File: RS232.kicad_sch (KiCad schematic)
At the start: 12 parts, among them Q5 BSS84, Q6 BSS84, U9 MAX3227

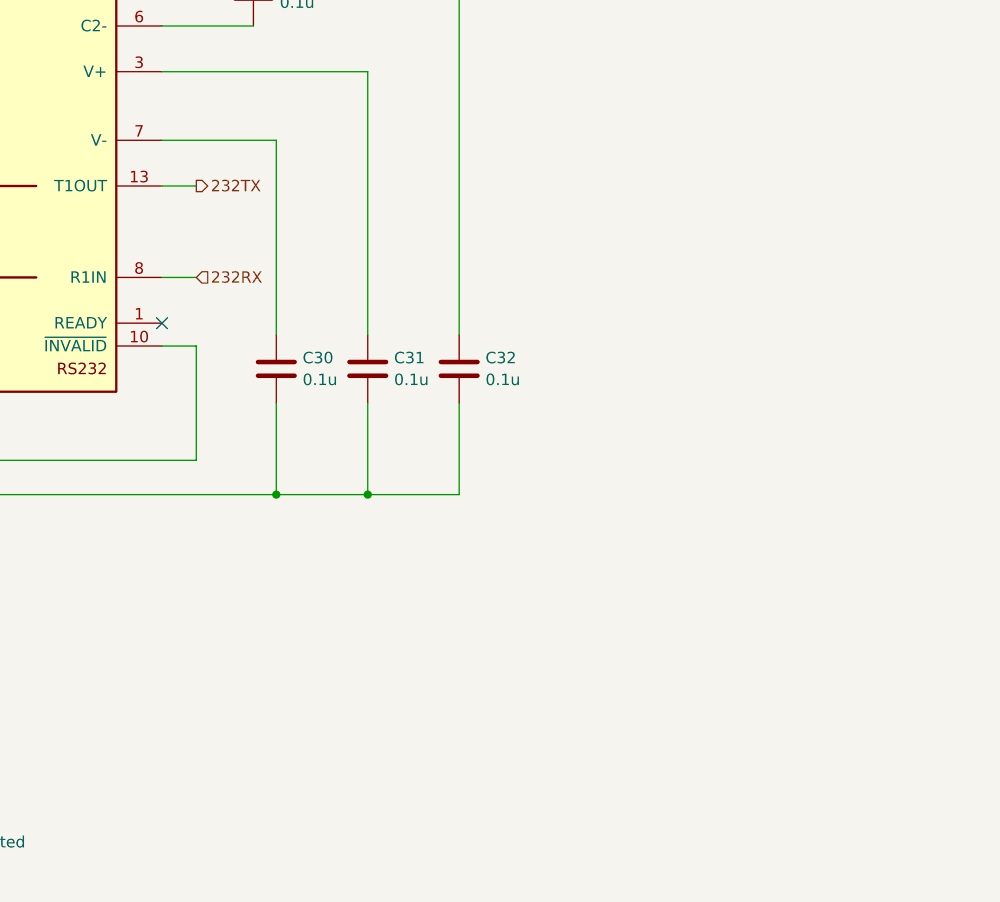
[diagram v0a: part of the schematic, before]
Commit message: added 4 inputs and 2 pwm outputs, completed routing
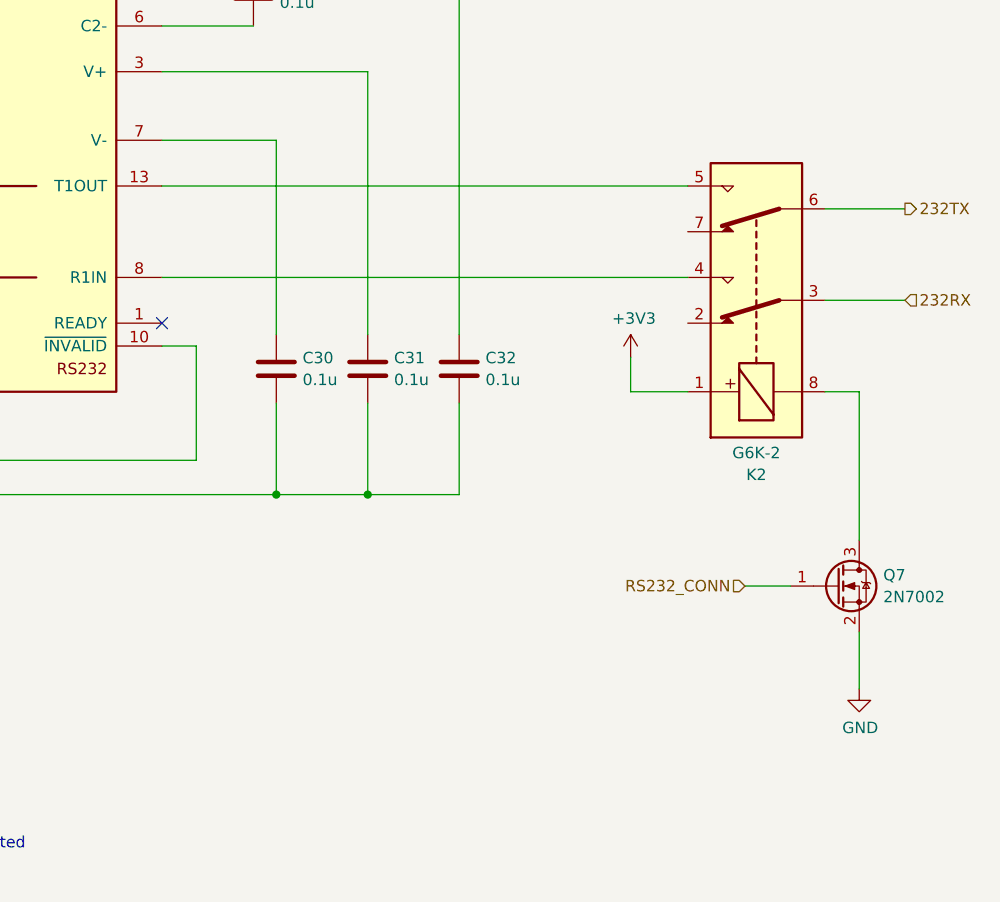
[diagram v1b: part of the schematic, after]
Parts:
- added K2: G6K-2, Relay_SMD:Relay_DPDT_Omron_G6K-2F, symbol Relay:G6K-2
- added Q7: 2N7002, Package_TO_SOT_SMD:SOT-23, symbol Transistor_FET:2N7002
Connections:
- net +3V3: now also K2.1
- net 232RX: now also K2.3; no longer U9.8 (R1IN)
- net 232TX: now also K2.6; no longer U9.13 (T1OUT)
- net GND: now also Q7.2 (S)
- new net: K2.5, U9.13 (T1OUT)
- new net: K2.4, U9.8 (R1IN)
- new net: K2.8, Q7.3 (D)
- new net RS232_CONN: Q7.1 (G)

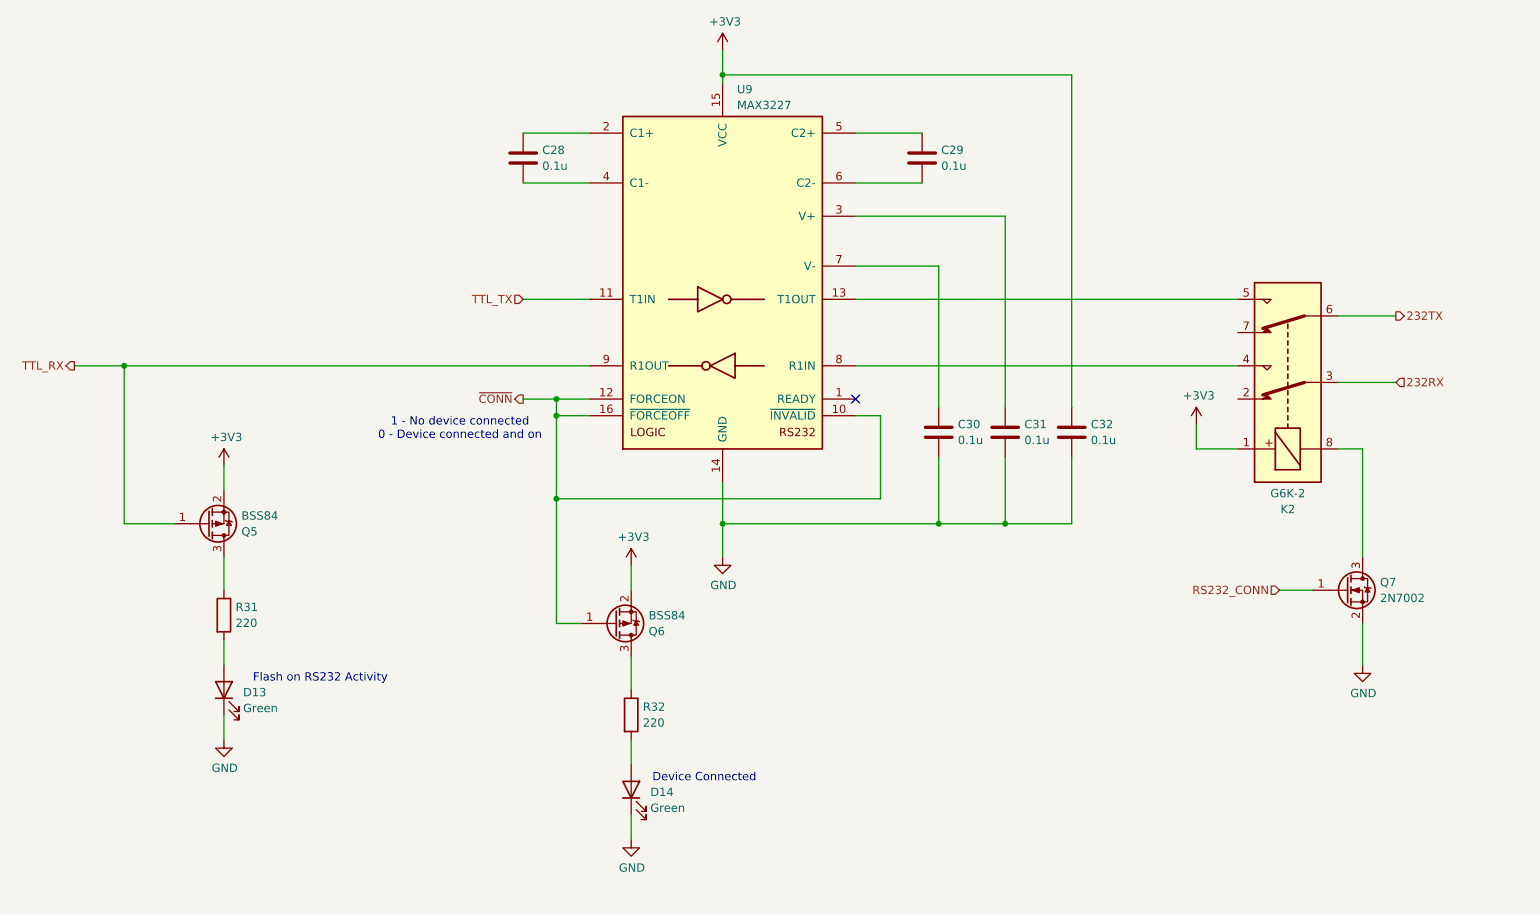
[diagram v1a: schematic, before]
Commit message: revised schematic after initial layout  - all connectors are vertical  - increased current handling of outputs  - replaced mechanical relay with ssr  - jumper to disable gps antenna power
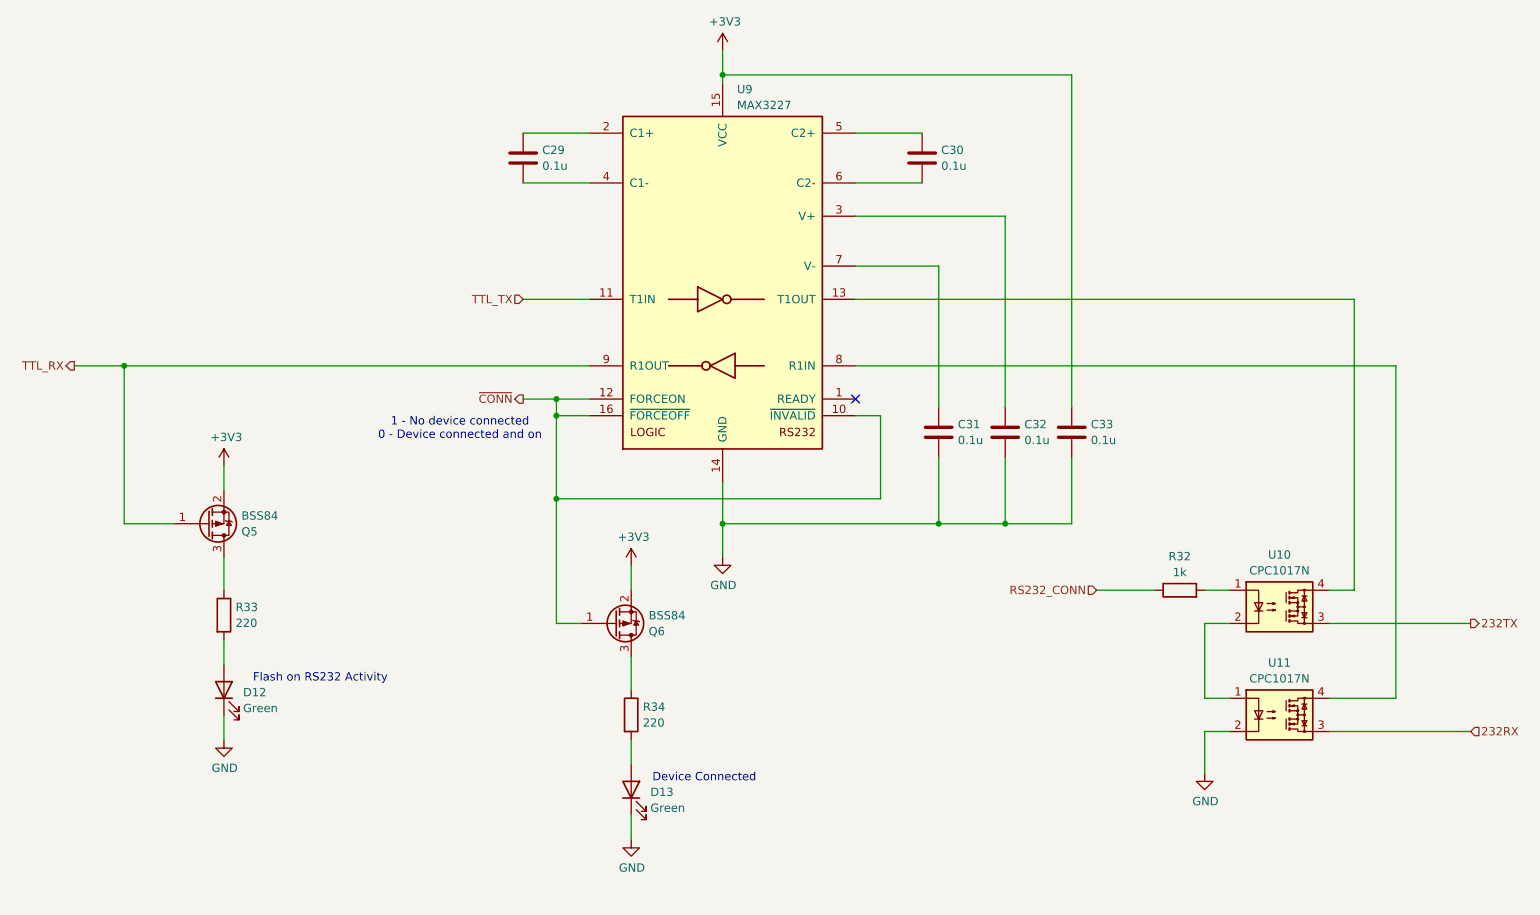
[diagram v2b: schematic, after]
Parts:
- removed K2: G6K-2, Relay_SMD:Relay_DPDT_Omron_G6K-2F, symbol Relay:G6K-2
- removed Q7: 2N7002, Package_TO_SOT_SMD:SOT-23, symbol Transistor_FET:2N7002
- added R32: 1k, Resistor_SMD:R_0603_1608Metric, symbol Device:R
- added U10, U11: CPC1017N, Package_SO:SOP-4_3.8x4.1mm_P2.54mm, symbol Relay_SolidState:CPC1017N
- C29: renamed from C28; footprint Capacitor_SMD:C_0603_1608Metric_Pad1.08x0.95mm_HandSolder -> Capacitor_SMD:C_0603_1608Metric
- C30: renamed from C29; footprint Capacitor_SMD:C_0603_1608Metric_Pad1.08x0.95mm_HandSolder -> Capacitor_SMD:C_0603_1608Metric
- C31: renamed from C30; footprint Capacitor_SMD:C_0603_1608Metric_Pad1.08x0.95mm_HandSolder -> Capacitor_SMD:C_0603_1608Metric
- C32: renamed from C31; footprint Capacitor_SMD:C_0603_1608Metric_Pad1.08x0.95mm_HandSolder -> Capacitor_SMD:C_0603_1608Metric
- C33: renamed from C32; footprint Capacitor_SMD:C_0603_1608Metric_Pad1.08x0.95mm_HandSolder -> Capacitor_SMD:C_0603_1608Metric
- D12: renamed from D13; footprint LED_SMD:LED_0603_1608Metric_Pad1.05x0.95mm_HandSolder -> LED_SMD:LED_0603_1608Metric
- D13: renamed from D14; footprint LED_SMD:LED_0603_1608Metric_Pad1.05x0.95mm_HandSolder -> LED_SMD:LED_0603_1608Metric
- R33: renamed from R31; footprint Resistor_SMD:R_0603_1608Metric_Pad0.98x0.95mm_HandSolder -> Resistor_SMD:R_0603_1608Metric
- R34: renamed from R32; footprint Resistor_SMD:R_0603_1608Metric_Pad0.98x0.95mm_HandSolder -> Resistor_SMD:R_0603_1608Metric
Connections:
- net 232RX: now also U11.3
- net 232TX: now also U10.3
- net GND: now also U11.2
- net RS232_CONN: now also R32.1
- net at U9.13 (T1OUT): now also U10.4
- net at U9.8 (R1IN): now also U11.4
- new net: R32.2, U10.1
- new net: U10.2, U11.1

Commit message: second pass at layout complete
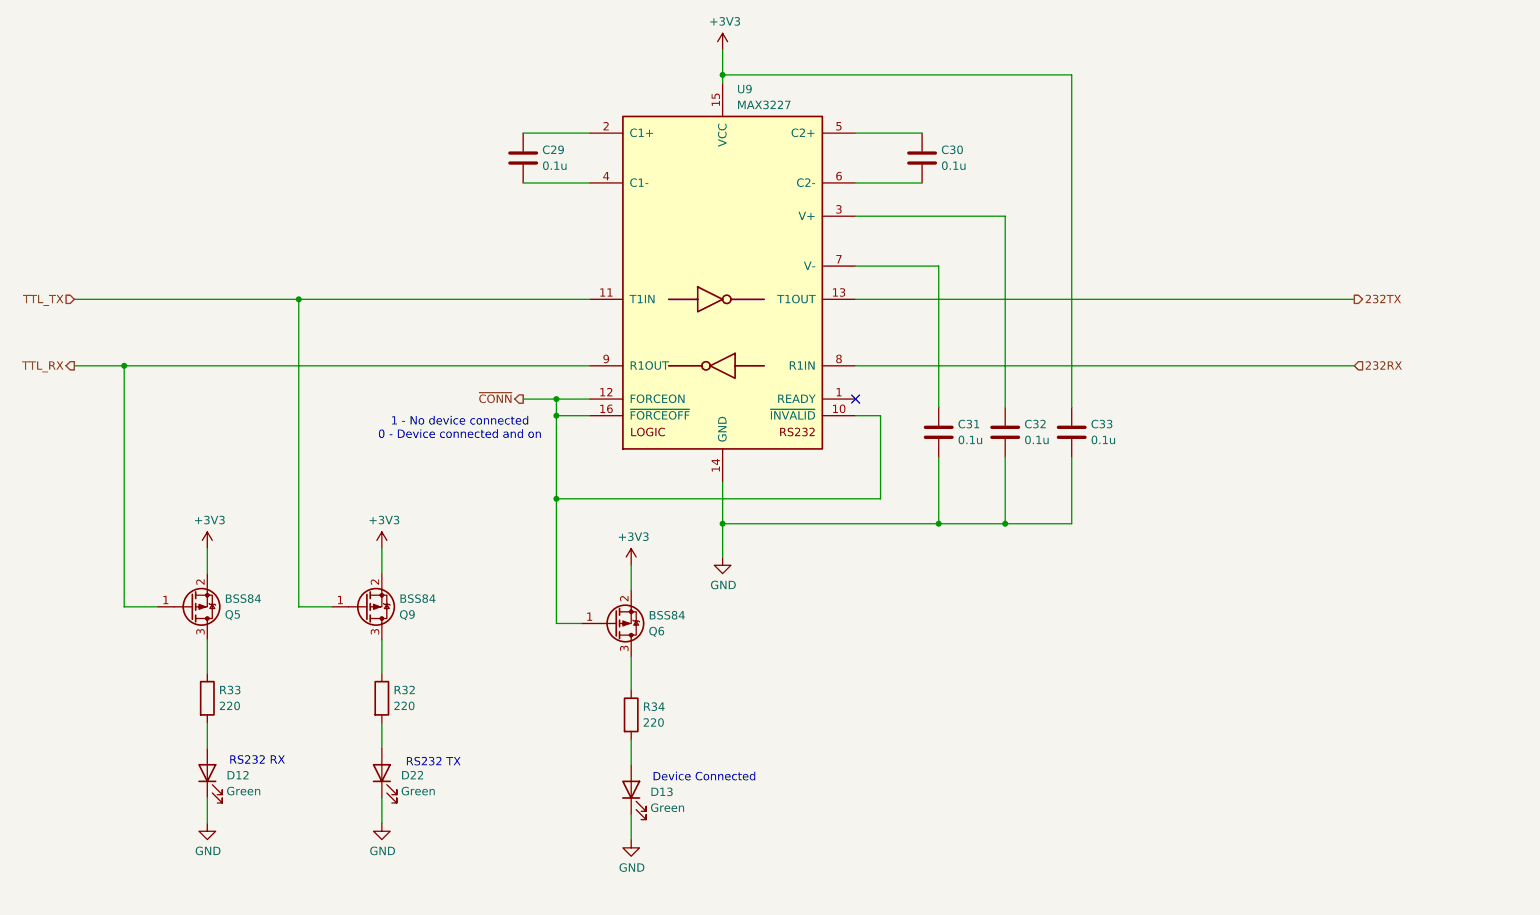
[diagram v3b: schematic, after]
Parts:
- removed U10, U11: CPC1017N, Package_SO:SOP-4_3.8x4.1mm_P2.54mm, symbol Relay_SolidState:CPC1017N
- added D22: Green, LED_SMD:LED_0603_1608Metric, symbol Device:LED
- added Q9: BSS84, Package_TO_SOT_SMD:SOT-23, symbol Transistor_FET:BSS84
- R32: value 1k -> 220
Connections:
- net +3V3: now also Q9.2 (S)
- net 232RX: now also U9.8 (R1IN)
- net 232TX: now also U9.13 (T1OUT)
- net GND: now also D22.1 (K)
- net TTL_TX: now also Q9.1 (G)
- net at R32.2: now also D22.2 (A)
- net RS232_CONN: no longer names the net of R32.1
- net RS232_CONN: now also Q9.3 (D)
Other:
- note added: "RS232 RX"
- note added: "RS232 TX"
- note removed: "Flash on RS232 Activity"
- moved on the sheet: D12, Q5, R33

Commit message: add a version, add uart test pads to gps, sent for manufacturing
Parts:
- Q5, Q6, Q9: Mfg Part Number BSS84 -> 2N7002
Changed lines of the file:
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@@
 			)
 		)
-		(property "Mfg Part Number" "BSS84"
+		(property "Mfg Part Number" "2N7002"
 			(at 46.99 128.27 0)
 			(effects
@@
 			)
 		)
-		(property "Mfg Part Number" "BSS84"
+		(property "Mfg Part Number" "2N7002"
 			(at 111.76 130.81 0)
 			(effects
@@
 			)
 		)
-		(property "Mfg Part Number" "BSS84"
+		(property "Mfg Part Number" "2N7002"
 			(at 73.66 128.27 0)
 			(effects

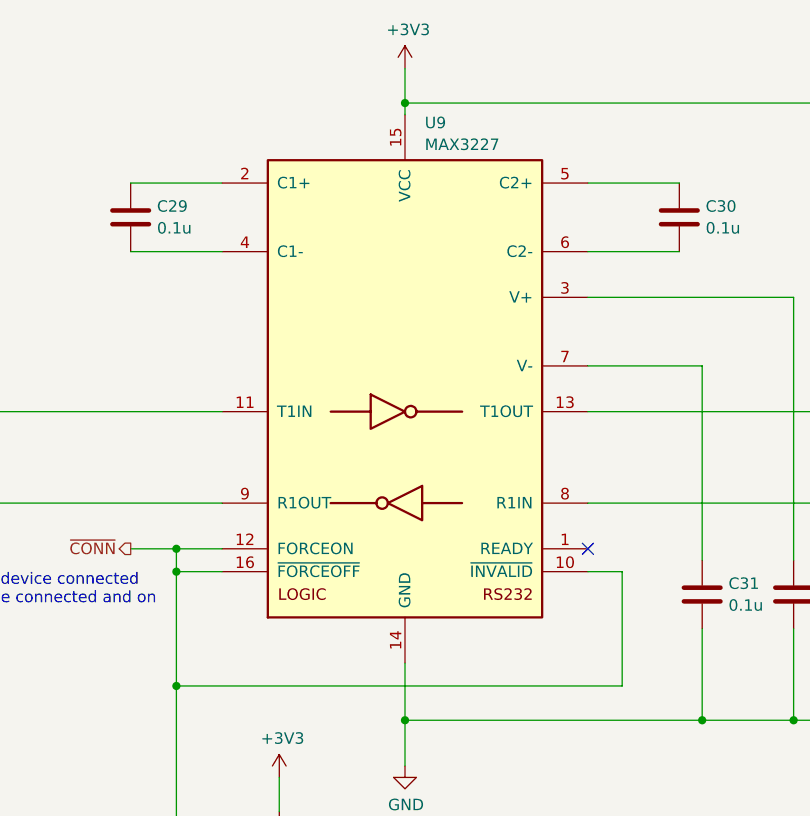
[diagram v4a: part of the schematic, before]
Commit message: bug fixes from testing
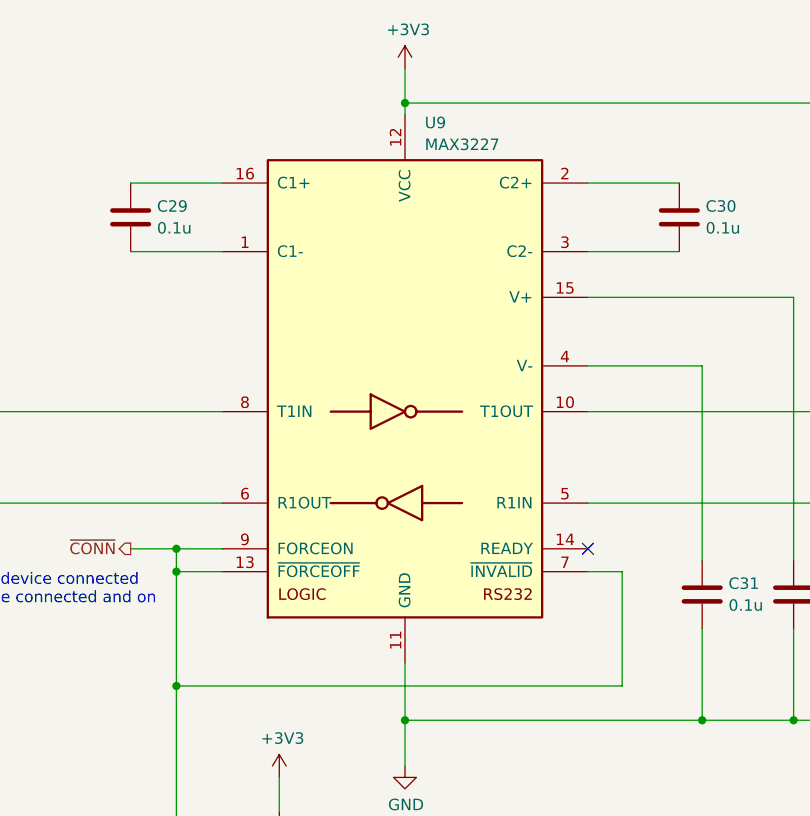
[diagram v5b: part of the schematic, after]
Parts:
- Q5, Q6, Q9: Mfg Part Number 2N7002 -> BSS84
- U9: symbol Interface_UART:MAX3227 -> Custom:MAX3226
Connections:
- net +3V3: now also U9.12 (VCC); no longer U9.15 (VCC)
- net 232RX: now also U9.5 (R1IN); no longer U9.8 (R1IN)
- net 232TX: now also U9.10 (T1OUT); no longer U9.13 (T1OUT)
- net GND: now also U9.11 (GND); no longer U9.14 (GND)
- net TTL_RX: now also U9.6 (R1OUT); no longer U9.9 (R1OUT)
- net TTL_TX: now also U9.8 (T1IN); no longer U9.11 (T1IN)
- net ~{CONN}: now also U9.13 (~{FORCEOFF}), U9.7 (~{INVALID}), U9.9 (FORCEON); no longer U9.10 (~{INVALID}), U9.12 (FORCEON), U9.16 (~{FORCEOFF})
- net at U9.1 (C1-): now also C29.2
- net at C29.1: now also U9.16 (C1+); no longer U9.2 (C1+)
- net at C32.1: now also U9.15 (V+); no longer U9.3 (V+)
- net at U9.4 (V-): now also C31.1; no longer C29.2
- net at C30.1: now also U9.2 (C2+); no longer U9.5 (C2+)
- net at C30.2: now also U9.3 (C2-); no longer U9.6 (C2-)
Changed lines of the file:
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@@
 			)
 		)
-		(property "Mfg Part Number" "2N7002"
+		(property "Mfg Part Number" "BSS84"
 			(at 46.99 128.27 0)
 			(effects
@@
 	)
 	(symbol
-		(lib_id "Interface_UART:MAX3227")
+		(lib_id "Custom:MAX3226")
 		(at 128.27 78.74 0)
 		(unit 1)
@@
 			)
 		)
-		(property "Description" "Single RS232 driver/receiver, 3.0V to 5V supply, 1Mb/s, AutoShutdown Plus, SSOP-16 package"
+		(property "Description" "Single RS232 driver/receiver, 3.0V to 5V supply, 250kb/s, AutoShutdown Plus, SSOP-16 package"
 			(at 128.27 78.74 0)
 			(effects
@@
 			)
 		)
-		(property "Mfg Part Number" "2N7002"
+		(property "Mfg Part Number" "BSS84"
 			(at 111.76 130.81 0)
 			(effects
@@
 			)
 		)
-		(property "Mfg Part Number" "2N7002"
+		(property "Mfg Part Number" "BSS84"
 			(at 73.66 128.27 0)
 			(effects
